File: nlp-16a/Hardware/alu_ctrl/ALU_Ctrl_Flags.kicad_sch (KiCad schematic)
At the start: 18 parts, among them U1 CD74HC00, U10 CD74HC00, U11 CD74HC00, U12 CD74HC00, U13 CD74HC00, U14 CD74HC00, U15 CD74HC00, U16 CD74HC00, U17 CD74HC00, U18 CD74HC00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

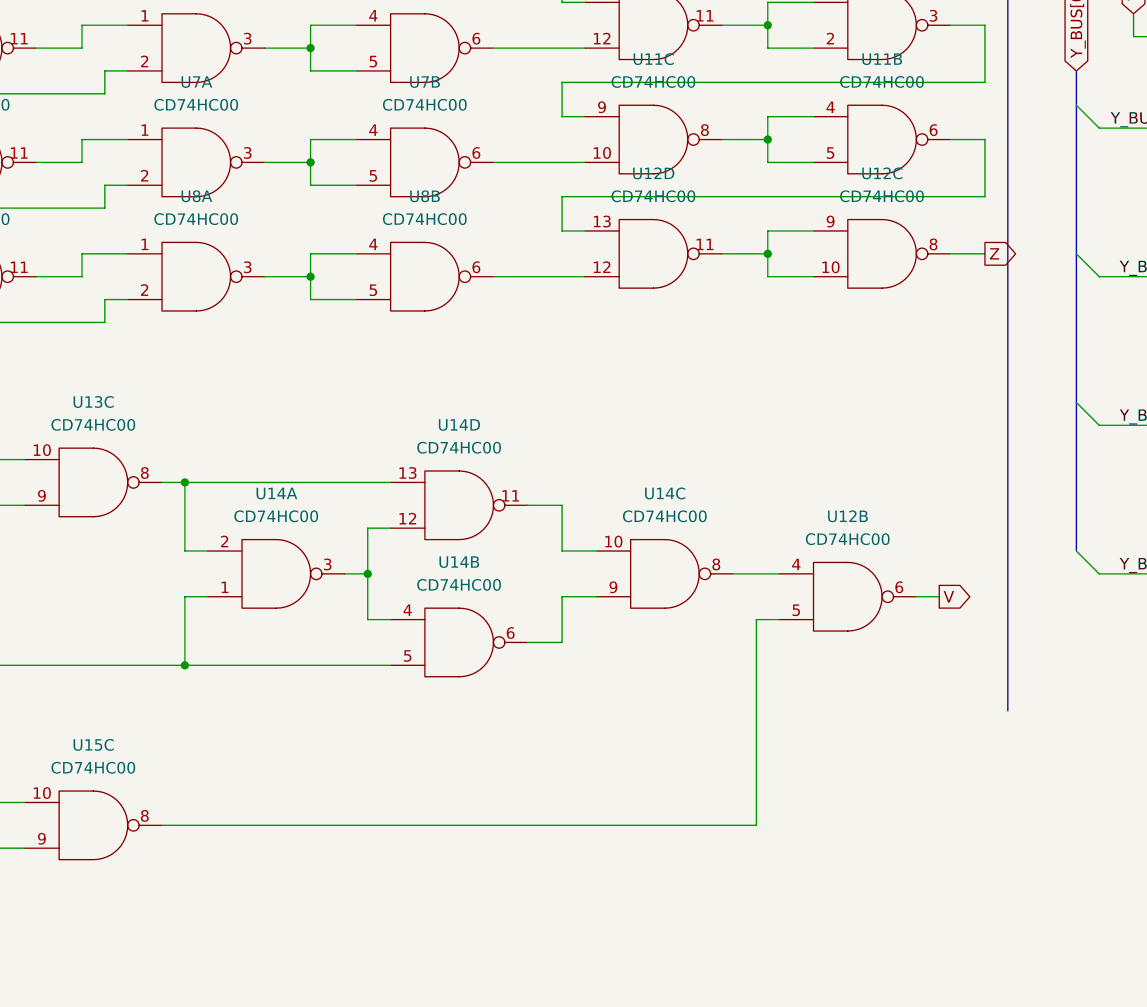
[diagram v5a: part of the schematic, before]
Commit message: オーバーフロー検出部修正
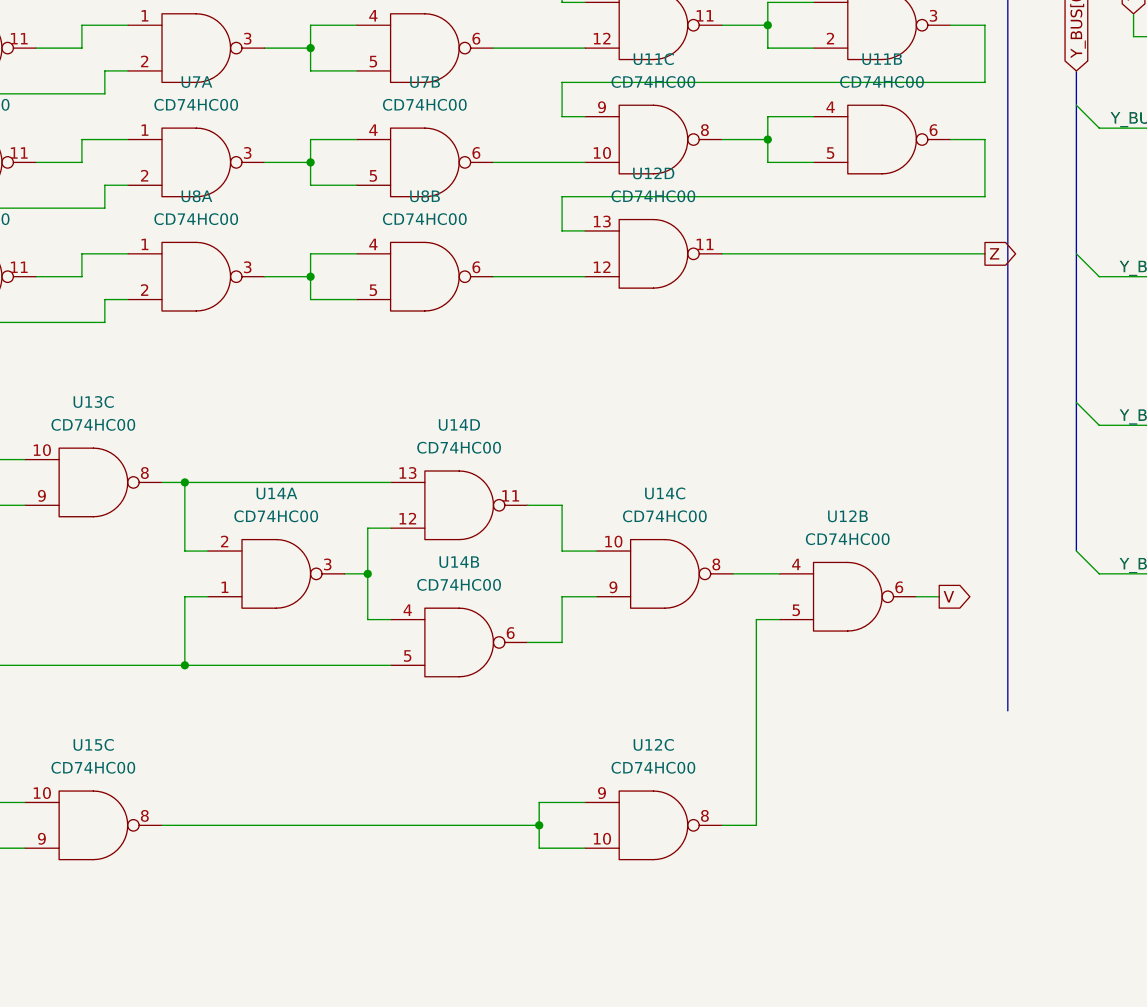
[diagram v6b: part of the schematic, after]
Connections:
- net Z: now also U12.11; no longer U12.8
- net at U12.5: now also U12.8; no longer U15.8
- net at U12.10, U12.9: now also U15.8; no longer U12.11
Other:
- moved on the sheet: U12C
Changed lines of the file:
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@@
   (junction (at 64.77 22.86) (diameter 0) (color 0 0 0 0)
   )
-  (junction (at 163.83 114.3) (diameter 0) (color 0 0 0 0)
+  (junction (at 138.43 177.8) (diameter 0) (color 0 0 0 0)
   )
   (junction (at 163.83 88.9) (diameter 0) (color 0 0 0 0)
@@
     (stroke (width 0) (type default) (color 0 0 0 0))
   )
+  (wire (pts (xy 187.96 114.3) (xy 158.75 114.3))
+    (stroke (width 0) (type default) (color 0 0 0 0))
+  )
   (wire (pts (xy 162.56 154.94) (xy 162.56 177.8))
     (stroke (width 0) (type default) (color 0 0 0 0))
@@
     (stroke (width 0) (type default) (color 0 0 0 0))
   )
-  (wire (pts (xy 163.83 116.84) (xy 168.91 116.84))
+  (wire (pts (xy 138.43 180.34) (xy 143.51 180.34))
     (stroke (width 0) (type default) (color 0 0 0 0))
   )
@@
     (stroke (width 0) (type default) (color 0 0 0 0))
   )
-  (wire (pts (xy 168.91 111.76) (xy 163.83 111.76))
+  (wire (pts (xy 143.51 175.26) (xy 138.43 175.26))
     (stroke (width 0) (type default) (color 0 0 0 0))
   )
@@
     (stroke (width 0) (type default) (color 0 0 0 0))
   )
-  (wire (pts (xy 158.75 114.3) (xy 163.83 114.3))
+  (wire (pts (xy 96.52 177.8) (xy 138.43 177.8))
     (stroke (width 0) (type default) (color 0 0 0 0))
   )
@@
     (stroke (width 0) (type default) (color 0 0 0 0))
   )
-  (wire (pts (xy 184.15 114.3) (xy 187.96 114.3))
+  (wire (pts (xy 158.75 177.8) (xy 162.56 177.8))
     (stroke (width 0) (type default) (color 0 0 0 0))
   )
@@
     (stroke (width 0) (type default) (color 0 0 0 0))
   )
-  (wire (pts (xy 163.83 111.76) (xy 163.83 114.3))
+  (wire (pts (xy 138.43 175.26) (xy 138.43 177.8))
     (stroke (width 0) (type default) (color 0 0 0 0))
   )
@@
     (stroke (width 0) (type default) (color 0 0 0 0))
   )
-  (wire (pts (xy 96.52 177.8) (xy 162.56 177.8))
-    (stroke (width 0) (type default) (color 0 0 0 0))
-  )
   (wire (pts (xy 113.03 78.74) (xy 113.03 76.2))
     (stroke (width 0) (type default) (color 0 0 0 0))
   )
-  (wire (pts (xy 163.83 114.3) (xy 163.83 116.84))
+  (wire (pts (xy 138.43 177.8) (xy 138.43 180.34))
     (stroke (width 0) (type default) (color 0 0 0 0))
   )
@@
   )
   (symbol (lib_id "CD74HCxx:CD74HC00") (at 152.4 149.86 0) (mirror x) (unit 3)
-    (in_bom yes) (on_board yes) (fields_autoplaced)
+    (in_bom yes) (on_board yes)
     (property "Reference" "U14" (id 0) (at 152.4 140.97 0))
     (property "Value" "CD74HC00" (id 1) (at 152.4 143.51 0))
@@
     (pin "13")
   )
-  (symbol (lib_id "CD74HCxx:CD74HC00") (at 176.53 114.3 0) (unit 3)
+  (symbol (lib_id "CD74HCxx:CD74HC00") (at 151.13 177.8 0) (unit 3)
     (in_bom yes) (on_board yes)
-    (property "Reference" "U12" (id 0) (at 176.53 105.41 0))
-    (property "Value" "CD74HC00" (id 1) (at 176.53 107.95 0))
-    (property "Footprint" "Package_DIP:DIP-14_W7.62mm" (id 2) (at 171.45 114.3 0)
-      (effects (font (size 1.27 1.27)) hide)
-    )
-    (property "Datasheet" "" (id 3) (at 171.45 114.3 0))
-    (pin "14")
-    (pin "7")
+    (property "Reference" "U12" (id 0) (at 151.13 168.91 0))
+    (property "Value" "CD74HC00" (id 1) (at 151.13 171.45 0))
+    (property "Footprint" "Package_DIP:DIP-14_W7.62mm" (id 2) (at 146.05 177.8 0)
+      (effects (font (size 1.27 1.27)) hide)
+    )
+    (property "Datasheet" "" (id 3) (at 146.05 177.8 0))
+    (pin "14")
+    (pin "7")

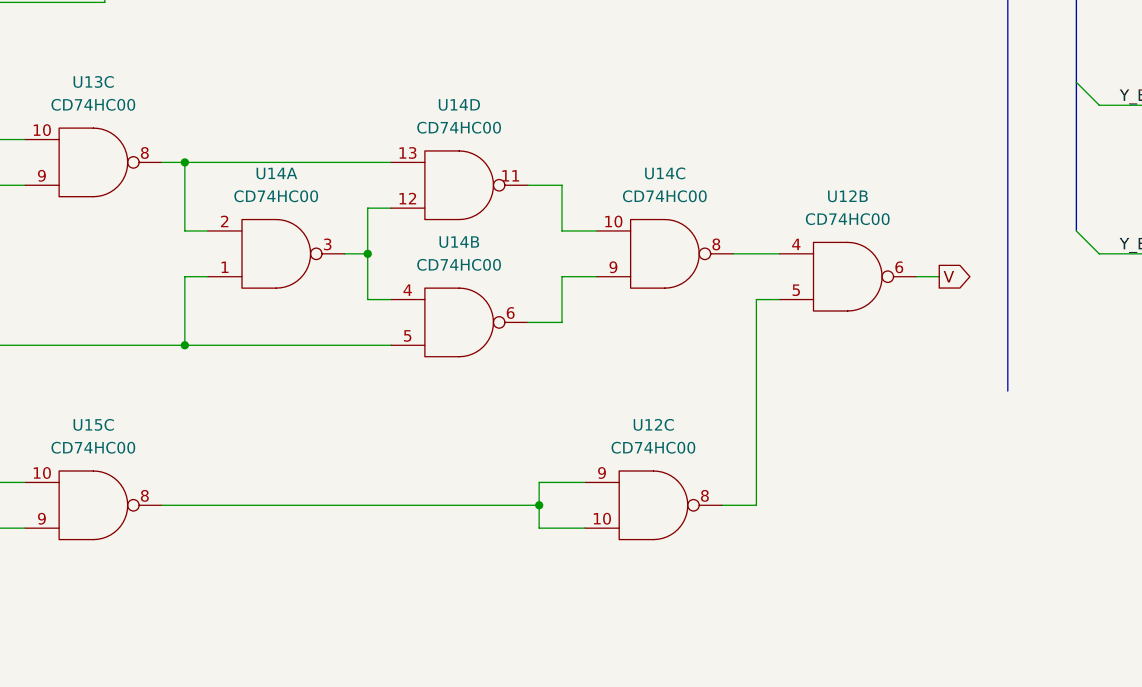
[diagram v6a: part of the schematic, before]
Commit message: 軽微な回路修正
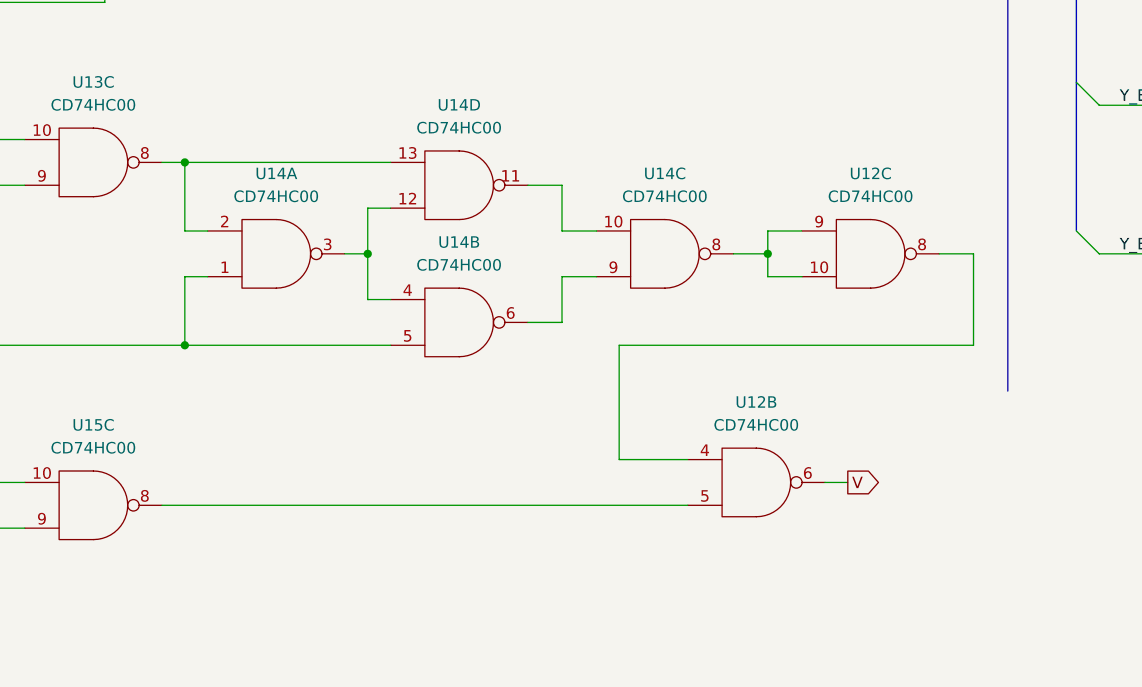
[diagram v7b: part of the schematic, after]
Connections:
- net at U12.4: now also U12.8; no longer U14.8
- net at U12.5: now also U15.8; no longer U12.8
- net at U12.10, U12.9: now also U14.8; no longer U15.8
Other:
- moved on the sheet: U12B, U12C
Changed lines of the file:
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@@
   (junction (at 64.77 22.86) (diameter 0) (color 0 0 0 0)
   )
-  (junction (at 138.43 177.8) (diameter 0) (color 0 0 0 0)
-  )
   (junction (at 163.83 88.9) (diameter 0) (color 0 0 0 0)
   )
@@
   (junction (at 35.56 187.96) (diameter 0) (color 0 0 0 0)
   )
+  (junction (at 163.83 149.86) (diameter 0) (color 0 0 0 0)
+  )
   (junction (at 163.83 50.8) (diameter 0) (color 0 0 0 0)
   )
@@
     (stroke (width 0) (type default) (color 0 0 0 0))
   )
+  (wire (pts (xy 186.69 149.86) (xy 186.69 160.02))
+    (stroke (width 0) (type default) (color 0 0 0 0))
+  )
   (wire (pts (xy 64.77 93.98) (xy 64.77 88.9))
     (stroke (width 0) (type default) (color 0 0 0 0))
@@
     (stroke (width 0) (type default) (color 0 0 0 0))
   )
+  (wire (pts (xy 96.52 177.8) (xy 154.94 177.8))
+    (stroke (width 0) (type default) (color 0 0 0 0))
+  )
   (wire (pts (xy 251.46 124.46) (xy 252.73 124.46))
     (stroke (width 0) (type default) (color 0 0 0 0))
@@
     (stroke (width 0) (type default) (color 0 0 0 0))
   )
-  (wire (pts (xy 162.56 154.94) (xy 162.56 177.8))
-    (stroke (width 0) (type default) (color 0 0 0 0))
-  )
   (wire (pts (xy 138.43 35.56) (xy 143.51 35.56))
     (stroke (width 0) (type default) (color 0 0 0 0))
@@
     (stroke (width 0) (type default) (color 0 0 0 0))
   )
-  (wire (pts (xy 138.43 180.34) (xy 143.51 180.34))
+  (wire (pts (xy 163.83 152.4) (xy 167.64 152.4))
     (stroke (width 0) (type default) (color 0 0 0 0))
   )
@@
     (stroke (width 0) (type default) (color 0 0 0 0))
   )
-  (wire (pts (xy 143.51 175.26) (xy 138.43 175.26))
+  (wire (pts (xy 167.64 147.32) (xy 163.83 147.32))
     (stroke (width 0) (type default) (color 0 0 0 0))
   )
@@
     (stroke (width 0) (type default) (color 0 0 0 0))
   )
-  (wire (pts (xy 96.52 177.8) (xy 138.43 177.8))
-    (stroke (width 0) (type default) (color 0 0 0 0))
-  )
   (wire (pts (xy 231.14 107.95) (xy 231.14 113.03))
     (stroke (width 0) (type default) (color 0 0 0 0))
@@
     (stroke (width 0) (type default) (color 0 0 0 0))
   )
-  (wire (pts (xy 158.75 177.8) (xy 162.56 177.8))
-    (stroke (width 0) (type default) (color 0 0 0 0))
-  )
   (wire (pts (xy 35.56 137.16) (xy 38.1 137.16))
     (stroke (width 0) (type default) (color 0 0 0 0))
@@
     (stroke (width 0) (type default) (color 0 0 0 0))
   )
-  (wire (pts (xy 180.34 152.4) (xy 182.88 152.4))
+  (wire (pts (xy 170.18 175.26) (xy 172.72 175.26))
     (stroke (width 0) (type default) (color 0 0 0 0))
   )
@@
     (stroke (width 0) (type default) (color 0 0 0 0))
   )
+  (wire (pts (xy 160.02 149.86) (xy 163.83 149.86))
+    (stroke (width 0) (type default) (color 0 0 0 0))
+  )
   (wire (pts (xy 234.95 138.43) (xy 234.95 133.35))
     (stroke (width 0) (type default) (color 0 0 0 0))
@@
     (stroke (width 0) (type default) (color 0 0 0 0))
   )
+  (wire (pts (xy 147.32 172.72) (xy 154.94 172.72))
+    (stroke (width 0) (type default) (color 0 0 0 0))
+  )
   (wire (pts (xy 163.83 86.36) (xy 168.91 86.36))
     (stroke (width 0) (type default) (color 0 0 0 0))
   )
+  (wire (pts (xy 186.69 160.02) (xy 147.32 160.02))
+    (stroke (width 0) (type default) (color 0 0 0 0))
+  )
   (wire (pts (xy 163.83 73.66) (xy 168.91 73.66))
     (stroke (width 0) (type default) (color 0 0 0 0))
@@
     (stroke (width 0) (type default) (color 0 0 0 0))
   )
-  (wire (pts (xy 138.43 175.26) (xy 138.43 177.8))
-    (stroke (width 0) (type default) (color 0 0 0 0))
-  )
   (wire (pts (xy 90.17 45.72) (xy 90.17 43.18))
     (stroke (width 0) (type default) (color 0 0 0 0))
@@
     (stroke (width 0) (type default) (color 0 0 0 0))
   )
-  (wire (pts (xy 165.1 154.94) (xy 162.56 154.94))
-    (stroke (width 0) (type default) (color 0 0 0 0))
-  )
   (wire (pts (xy 168.91 66.04) (xy 163.83 66.04))
     (stroke (width 0) (type default) (color 0 0 0 0))
@@
     (stroke (width 0) (type default) (color 0 0 0 0))
   )
+  (wire (pts (xy 182.88 149.86) (xy 186.69 149.86))
+    (stroke (width 0) (type default) (color 0 0 0 0))
+  )
   (wire (pts (xy 36.83 104.14) (xy 36.83 106.68))
     (stroke (width 0) (type default) (color 0 0 0 0))
@@
     (stroke (width 0) (type default) (color 0 0 0 0))
   )
-  (wire (pts (xy 160.02 149.86) (xy 165.1 149.86))
-    (stroke (width 0) (type default) (color 0 0 0 0))
-  )
   (wire (pts (xy 31.75 160.02) (xy 31.75 167.64))
     (stroke (width 0) (type default) (color 0 0 0 0))
@@
     (stroke (width 0) (type default) (color 0 0 0 0))
   )
+  (wire (pts (xy 163.83 149.86) (xy 163.83 152.4))
+    (stroke (width 0) (type default) (color 0 0 0 0))
+  )
   (wire (pts (xy 35.56 167.64) (xy 58.42 167.64))
     (stroke (width 0) (type default) (color 0 0 0 0))
@@
     (stroke (width 0) (type default) (color 0 0 0 0))
   )
-  (wire (pts (xy 138.43 177.8) (xy 138.43 180.34))
+  (wire (pts (xy 163.83 147.32) (xy 163.83 149.86))
     (stroke (width 0) (type default) (color 0 0 0 0))
   )
@@
   )
   (wire (pts (xy 36.83 43.18) (xy 41.91 43.18))
+    (stroke (width 0) (type default) (color 0 0 0 0))
+  )
+  (wire (pts (xy 147.32 160.02) (xy 147.32 172.72))
     (stroke (width 0) (type default) (color 0 0 0 0))
   )
@@
     )
   )
-  (global_label "V" (shape output) (at 182.88 152.4 0) (fields_autoplaced)
+  (global_label "V" (shape output) (at 172.72 175.26 0) (fields_autoplaced)
     (effects (font (size 1.27 1.27)) (justify left))
-    (property "Intersheet References" "${INTERSHEET_REFS}" (id 0) (at 186.3817 152.3206 0)
+    (property "Intersheet References" "${INTERSHEET_REFS}" (id 0) (at 176.2217 175.1806 0)
       (effects (font (size 1.27 1.27)) (justify left) hide)
     )
@@
     (pin "13")
   )
-  (symbol (lib_id "CD74HCxx:CD74HC00") (at 172.72 152.4 0) (unit 2)
-    (in_bom yes) (on_board yes) (fields_autoplaced)
-    (property "Reference" "U12" (id 0) (at 172.72 143.51 0))
-    (property "Value" "CD74HC00" (id 1) (at 172.72 146.05 0))
-    (property "Footprint" "Package_DIP:DIP-14_W7.62mm" (id 2) (at 167.64 152.4 0)
-      (effects (font (size 1.27 1.27)) hide)
-    )
-    (property "Datasheet" "" (id 3) (at 167.64 152.4 0))
+  (symbol (lib_id "CD74HCxx:CD74HC00") (at 162.56 175.26 0) (unit 2)
+    (in_bom yes) (on_board yes) (fields_autoplaced)
+    (property "Reference" "U12" (id 0) (at 162.56 166.37 0))
+    (property "Value" "CD74HC00" (id 1) (at 162.56 168.91 0))
+    (property "Footprint" "Package_DIP:DIP-14_W7.62mm" (id 2) (at 157.48 175.26 0)
+      (effects (font (size 1.27 1.27)) hide)
+    )
+    (property "Datasheet" "" (id 3) (at 157.48 175.26 0))
     (pin "14")
     (pin "7")
@@
     (pin "13")
   )
-  (symbol (lib_id "CD74HCxx:CD74HC00") (at 151.13 177.8 0) (unit 3)
+  (symbol (lib_id "CD74HCxx:CD74HC00") (at 175.26 149.86 0) (unit 3)
     (in_bom yes) (on_board yes)
-    (property "Reference" "U12" (id 0) (at 151.13 168.91 0))
-    (property "Value" "CD74HC00" (id 1) (at 151.13 171.45 0))
-    (property "Footprint" "Package_DIP:DIP-14_W7.62mm" (id 2) (at 146.05 177.8 0)
-      (effects (font (size 1.27 1.27)) hide)
-    )
-    (property "Datasheet" "" (id 3) (at 146.05 177.8 0))
-    (pin "14")
-    (pin "7")
+    (property "Reference" "U12" (id 0) (at 175.26 140.97 0))
+    (property "Value" "CD74HC00" (id 1) (at 175.26 143.51 0))
+    (property "Footprint" "Package_DIP:DIP-14_W7.62mm" (id 2) (at 170.18 149.86 0)
+      (effects (font (size 1.27 1.27)) hide)
+    )
+    (property "Datasheet" "" (id 3) (at 170.18 149.86 0))
+    (pin "14")
+    (pin "7")

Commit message: 先ほどのオーバーフロー検出部の不具合を修正
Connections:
- net Y_BUS15: no longer U16.1
- net at U1.1, U1.11: now also U16.1
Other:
- note added: "フラグのSVZは反転して負論理で格納． フラグ選択の回路で通常時に反転させることでフラグの動作を正論理で扱えるようにする (Cフラグのみプログラムでの修正が必要だが使っていないため問題ない)"
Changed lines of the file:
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@@
   (junction (at 36.83 40.64) (diameter 0) (color 0 0 0 0)
   )
-  (junction (at 64.77 22.86) (diameter 0) (color 0 0 0 0)
-  )
   (junction (at 163.83 88.9) (diameter 0) (color 0 0 0 0)
   )
@@
   (junction (at 36.83 53.34) (diameter 0) (color 0 0 0 0)
   )
+  (junction (at 87.63 25.4) (diameter 0) (color 0 0 0 0)
+  )
   (junction (at 212.09 90.17) (diameter 0) (color 0 0 0 0)
   )
@@
     (stroke (width 0) (type default) (color 0 0 0 0))
   )
+  (wire (pts (xy 87.63 22.86) (xy 209.55 22.86))
+    (stroke (width 0) (type default) (color 0 0 0 0))
+  )
   (wire (pts (xy 99.06 147.32) (xy 101.6 147.32))
     (stroke (width 0) (type default) (color 0 0 0 0))
@@
     (stroke (width 0) (type default) (color 0 0 0 0))
   )
-  (wire (pts (xy 64.77 22.86) (xy 209.55 22.86))
-    (stroke (width 0) (type default) (color 0 0 0 0))
-  )
   (wire (pts (xy 163.83 149.86) (xy 163.83 152.4))
     (stroke (width 0) (type default) (color 0 0 0 0))
@@
   )
   (wire (pts (xy 140.97 44.45) (xy 187.96 44.45))
+    (stroke (width 0) (type default) (color 0 0 0 0))
+  )
+  (wire (pts (xy 87.63 25.4) (xy 87.63 22.86))
     (stroke (width 0) (type default) (color 0 0 0 0))
   )
@@
     (effects (font (size 1.27 1.27)) (justify left bottom))
   )
+  (text "フラグのSVZは反転して負論理で格納．\nフラグ選択の回路で通常時に反転させることでフラグの動作を正論理で扱えるようにする\n(Cフラグのみプログラムでの修正が必要だが使っていないため問題ない)"
+    (at 196.85 167.64 0)
+    (effects (font (size 1.27 1.27)) (justify left bottom))
+  )
